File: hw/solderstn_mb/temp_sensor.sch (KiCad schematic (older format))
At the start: 2 parts, among them U901 TMP100

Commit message: Corrected several ERC issues. Re-annotated & assigned all footprints except 32k xtal (will prob. replace with RTC module anyway)
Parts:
- U901: footprint Package_TO_SOT_SMD:SOT-23-6 -> Package_TO_SOT_SMD:SOT-23-6_Handsoldering
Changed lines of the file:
@@
 F 0 "U1101" H 2550 3000 50  0000 C CNN
 F 1 "TMP100" H 2650 2300 50  0000 C CNN
-F 2 "Package_TO_SOT_SMD:SOT-23-6" H 2400 2300 50  0001 C CNN
+F 2 "Package_TO_SOT_SMD:SOT-23-6_Handsoldering" H 2400 2300 50  0001 C CNN
 F 3 "http://www.ti.com/lit/gpn/tmp100" H 2350 2650 50  0001 C CNN
 	1    2400 2650

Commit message: MB - Sch design: VS1063 in new audio path; Added: some new ESD, some fixups; Changes: some footprints, fixes
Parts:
- U901: footprint Package_TO_SOT_SMD:SOT-23-6_Handsoldering -> Package_TO_SOT_SMD:TSOT-23-6
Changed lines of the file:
@@
 $Descr A4 11693 8268
 encoding utf-8
-Sheet 11 21
+Sheet 7 21
 Title ""
 Date ""
@@
 F 0 "U1101" H 2550 3000 50  0000 C CNN
 F 1 "TMP100" H 2650 2300 50  0000 C CNN
-F 2 "Package_TO_SOT_SMD:SOT-23-6_Handsoldering" H 2400 2300 50  0001 C CNN
+F 2 "Package_TO_SOT_SMD:TSOT-23-6" H 2400 2300 50  0001 C CNN
 F 3 "http://www.ti.com/lit/gpn/tmp100" H 2350 2650 50  0001 C CNN
 	1    2400 2650

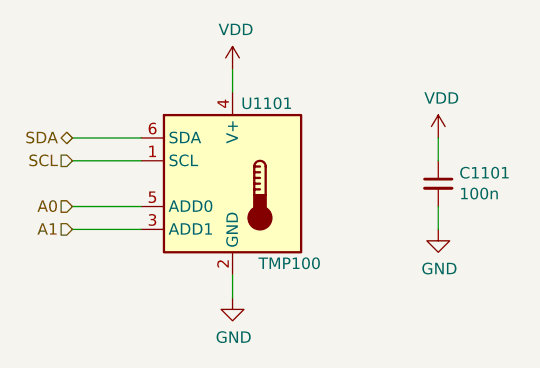
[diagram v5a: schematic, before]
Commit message: Reannotate entire schematic; add temp.extra SMA-conn to eval alternative FMI placement
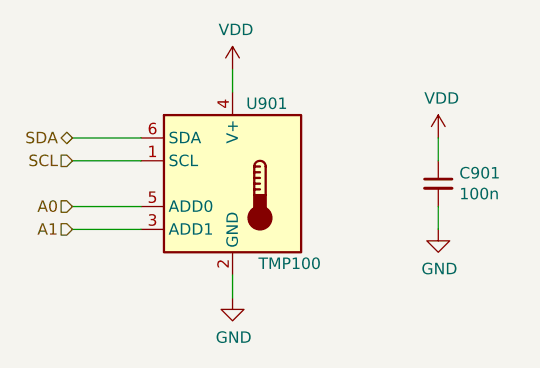
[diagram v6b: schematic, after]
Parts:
- renumbered C901 to C701, U901 to U701
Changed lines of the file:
@@
 AR Path="/5F2BE47E/5F4C3A03" Ref="U?"  Part="1"
 AR Path="/5F2C0DB1/5F4C3A03" Ref="U?"  Part="1"
-AR Path="/5F472FC2/5F4B6AEC/5F4C3A03" Ref="U901"  Part="1"
-AR Path="/5F472FC2/5F4B6CAA/5F4C3A03" Ref="U1001"  Part="1"
-AR Path="/5F472FC2/5F4B6E36/5F4C3A03" Ref="U1101"  Part="1"
-F 0 "U1101" H 2550 3000 50  0000 C CNN
+AR Path="/5F472FC2/5F4B6AEC/5F4C3A03" Ref="U701"  Part="1"
+AR Path="/5F472FC2/5F4B6CAA/5F4C3A03" Ref="U801"  Part="1"
+AR Path="/5F472FC2/5F4B6E36/5F4C3A03" Ref="U901"  Part="1"
+F 0 "U901" H 2550 3000 50  0000 C CNN
 F 1 "TMP100" H 2650 2300 50  0000 C CNN
 F 2 "Package_TO_SOT_SMD:TSOT-23-6" H 2400 2300 50  0001 C CNN
@@
 AR Path="/5F2BE47E/5F4C3A04" Ref="#PWR?"  Part="1"
 AR Path="/5F2C0DB1/5F4C3A04" Ref="#PWR?"  Part="1"
-AR Path="/5F472FC2/5F4B6AEC/5F4C3A04" Ref="#PWR0904"  Part="1"
-AR Path="/5F472FC2/5F4B6CAA/5F4C3A04" Ref="#PWR01004"  Part="1"
-AR Path="/5F472FC2/5F4B6E36/5F4C3A04" Ref="#PWR01104"  Part="1"
-F 0 "#PWR01104" H 2400 2900 50  0001 C CNN
+AR Path="/5F472FC2/5F4B6AEC/5F4C3A04" Ref="#PWR0704"  Part="1"
+AR Path="/5F472FC2/5F4B6CAA/5F4C3A04" Ref="#PWR0804"  Part="1"
+AR Path="/5F472FC2/5F4B6E36/5F4C3A04" Ref="#PWR0904"  Part="1"
+F 0 "#PWR0904" H 2400 2900 50  0001 C CNN
 F 1 "GND" H 2405 2977 50  0000 C CNN
 F 2 "" H 2400 3150 50  0001 C CNN
@@
 AR Path="/5F2BE47E/5F4C3A05" Ref="C?"  Part="1"
 AR Path="/5F2C0DB1/5F4C3A05" Ref="C?"  Part="1"
-AR Path="/5F472FC2/5F4B6AEC/5F4C3A05" Ref="C901"  Part="1"
-AR Path="/5F472FC2/5F4B6CAA/5F4C3A05" Ref="C1001"  Part="1"
-AR Path="/5F472FC2/5F4B6E36/5F4C3A05" Ref="C1101"  Part="1"
-F 0 "C1101" H 3392 2696 50  0000 L CNN
+AR Path="/5F472FC2/5F4B6AEC/5F4C3A05" Ref="C701"  Part="1"
+AR Path="/5F472FC2/5F4B6CAA/5F4C3A05" Ref="C801"  Part="1"
+AR Path="/5F472FC2/5F4B6E36/5F4C3A05" Ref="C901"  Part="1"
+F 0 "C901" H 3392 2696 50  0000 L CNN
 F 1 "100n" H 3392 2605 50  0000 L CNN
 F 2 "Capacitor_SMD:C_0603_1608Metric" H 3300 2650 50  0001 C CNN
@@
 AR Path="/5F2BE47E/5F2B588B" Ref="#PWR?"  Part="1"
 AR Path="/5F2C0DB1/5F2B588B" Ref="#PWR?"  Part="1"
-AR Path="/5F472FC2/5F4B6AEC/5F2B588B" Ref="#PWR0903"  Part="1"
-AR Path="/5F472FC2/5F4B6CAA/5F2B588B" Ref="#PWR01003"  Part="1"
-AR Path="/5F472FC2/5F4B6E36/5F2B588B" Ref="#PWR01103"  Part="1"
-F 0 "#PWR01103" H 3300 2600 50  0001 C CNN
+AR Path="/5F472FC2/5F4B6AEC/5F2B588B" Ref="#PWR0703"  Part="1"
+AR Path="/5F472FC2/5F4B6CAA/5F2B588B" Ref="#PWR0803"  Part="1"
+AR Path="/5F472FC2/5F4B6E36/5F2B588B" Ref="#PWR0903"  Part="1"
+F 0 "#PWR0903" H 3300 2600 50  0001 C CNN
 F 1 "GND" H 3305 2677 50  0000 C CNN
 F 2 "" H 3300 2850 50  0001 C CNN
@@
 	3300 2850 3300 2750
 $Comp
-L power:VDD #PWR0901
+L power:VDD #PWR0701
 U 1 1 5F4B752F
 P 2400 2150
-AR Path="/5F472FC2/5F4B6AEC/5F4B752F" Ref="#PWR0901"  Part="1"
-AR Path="/5F472FC2/5F4B6CAA/5F4B752F" Ref="#PWR01001"  Part="1"
-AR Path="/5F472FC2/5F4B6E36/5F4B752F" Ref="#PWR01101"  Part="1"
-F 0 "#PWR01101" H 2400 2000 50  0001 C CNN
+AR Path="/5F472FC2/5F4B6AEC/5F4B752F" Ref="#PWR0701"  Part="1"
+AR Path="/5F472FC2/5F4B6CAA/5F4B752F" Ref="#PWR0801"  Part="1"
+AR Path="/5F472FC2/5F4B6E36/5F4B752F" Ref="#PWR0901"  Part="1"
+F 0 "#PWR0901" H 2400 2000 50  0001 C CNN
 F 1 "VDD" H 2415 2323 50  0000 C CNN
 F 2 "" H 2400 2150 50  0001 C CNN
@@
 $EndComp
 $Comp
-L power:VDD #PWR0902
+L power:VDD #PWR0702
 U 1 1 5F4B7A67
 P 3300 2450
-AR Path="/5F472FC2/5F4B6AEC/5F4B7A67" Ref="#PWR0902"  Part="1"
-AR Path="/5F472FC2/5F4B6CAA/5F4B7A67" Ref="#PWR01002"  Part="1"
-AR Path="/5F472FC2/5F4B6E36/5F4B7A67" Ref="#PWR01102"  Part="1"
-F 0 "#PWR01102" H 3300 2300 50  0001 C CNN
+AR Path="/5F472FC2/5F4B6AEC/5F4B7A67" Ref="#PWR0702"  Part="1"
+AR Path="/5F472FC2/5F4B6CAA/5F4B7A67" Ref="#PWR0802"  Part="1"
+AR Path="/5F472FC2/5F4B6E36/5F4B7A67" Ref="#PWR0902"  Part="1"
+F 0 "#PWR0902" H 3300 2300 50  0001 C CNN
 F 1 "VDD" H 3315 2623 50  0000 C CNN
 F 2 "" H 3300 2450 50  0001 C CNN

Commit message: MB: major update of footprints, LCSC part numbers and Basic/Extended library indicator, for _most_ of the BoM. (Also removed JP1101/JP1102, bypass jmprs)
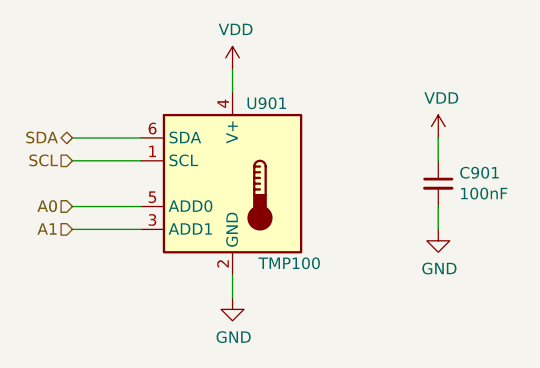
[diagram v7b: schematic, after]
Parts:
- C701: value 100n -> 100nF; footprint Capacitor_SMD:C_0603_1608Metric -> Capacitor_SMD:C_0402_1005Metric; JLC_part (none) -> Basic; LCSC (none) -> C1525
- U701: JLC_part (none) -> Extended; LCSC (none) -> C31810
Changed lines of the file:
@@
 F 2 "Package_TO_SOT_SMD:TSOT-23-6" H 2400 2300 50  0001 C CNN
 F 3 "http://www.ti.com/lit/gpn/tmp100" H 2350 2650 50  0001 C CNN
+F 4 "Extended" H 2400 2650 50  0001 C CNN "JLC_part"
+F 5 "C31810" H 2400 2650 50  0001 C CNN "LCSC"
 	1    2400 2650
 	1    0    0    -1
@@
 AR Path="/5F472FC2/5F4B6E36/5F4C3A05" Ref="C901"  Part="1"
 F 0 "C901" H 3392 2696 50  0000 L CNN
-F 1 "100n" H 3392 2605 50  0000 L CNN
-F 2 "Capacitor_SMD:C_0603_1608Metric" H 3300 2650 50  0001 C CNN
+F 1 "100nF" H 3392 2605 50  0000 L CNN
+F 2 "Capacitor_SMD:C_0402_1005Metric" H 3300 2650 50  0001 C CNN
 F 3 "~" H 3300 2650 50  0001 C CNN
+F 4 "Basic" H 3300 2650 50  0001 C CNN "JLC_part"
+F 5 "C1525" H 3300 2650 50  0001 C CNN "LCSC"
 	1    3300 2650
 	1    0    0    -1

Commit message: solderstn_mb : Misc uncommitted changes I dont remember...
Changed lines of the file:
@@
 AR Path="/5F472FC2/5F4B6CAA/5F4C3A03" Ref="U801"  Part="1"
 AR Path="/5F472FC2/5F4B6E36/5F4C3A03" Ref="U901"  Part="1"
-F 0 "U901" H 2550 3000 50  0000 C CNN
+F 0 "U701" H 2550 3000 50  0000 C CNN
 F 1 "TMP100" H 2650 2300 50  0000 C CNN
 F 2 "Package_TO_SOT_SMD:TSOT-23-6" H 2400 2300 50  0001 C CNN
@@
 AR Path="/5F472FC2/5F4B6CAA/5F4C3A04" Ref="#PWR0804"  Part="1"
 AR Path="/5F472FC2/5F4B6E36/5F4C3A04" Ref="#PWR0904"  Part="1"
-F 0 "#PWR0904" H 2400 2900 50  0001 C CNN
+F 0 "#PWR0704" H 2400 2900 50  0001 C CNN
 F 1 "GND" H 2405 2977 50  0000 C CNN
 F 2 "" H 2400 3150 50  0001 C CNN
@@
 AR Path="/5F472FC2/5F4B6CAA/5F4C3A05" Ref="C801"  Part="1"
 AR Path="/5F472FC2/5F4B6E36/5F4C3A05" Ref="C901"  Part="1"
-F 0 "C901" H 3392 2696 50  0000 L CNN
+F 0 "C701" H 3392 2696 50  0000 L CNN
 F 1 "100nF" H 3392 2605 50  0000 L CNN
 F 2 "Capacitor_SMD:C_0402_1005Metric" H 3300 2650 50  0001 C CNN
@@
 AR Path="/5F472FC2/5F4B6CAA/5F2B588B" Ref="#PWR0803"  Part="1"
 AR Path="/5F472FC2/5F4B6E36/5F2B588B" Ref="#PWR0903"  Part="1"
-F 0 "#PWR0903" H 3300 2600 50  0001 C CNN
+F 0 "#PWR0703" H 3300 2600 50  0001 C CNN
 F 1 "GND" H 3305 2677 50  0000 C CNN
 F 2 "" H 3300 2850 50  0001 C CNN
@@
 AR Path="/5F472FC2/5F4B6CAA/5F4B752F" Ref="#PWR0801"  Part="1"
 AR Path="/5F472FC2/5F4B6E36/5F4B752F" Ref="#PWR0901"  Part="1"
-F 0 "#PWR0901" H 2400 2000 50  0001 C CNN
+F 0 "#PWR0701" H 2400 2000 50  0001 C CNN
 F 1 "VDD" H 2415 2323 50  0000 C CNN
 F 2 "" H 2400 2150 50  0001 C CNN
@@
 AR Path="/5F472FC2/5F4B6CAA/5F4B7A67" Ref="#PWR0802"  Part="1"
 AR Path="/5F472FC2/5F4B6E36/5F4B7A67" Ref="#PWR0902"  Part="1"
-F 0 "#PWR0902" H 3300 2300 50  0001 C CNN
+F 0 "#PWR0702" H 3300 2300 50  0001 C CNN
 F 1 "VDD" H 3315 2623 50  0000 C CNN
 F 2 "" H 3300 2450 50  0001 C CNN
